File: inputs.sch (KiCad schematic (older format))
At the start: 72 parts, among them P29 .., P30 ., U4 MAX9926UAEE+, U5 74LS86, U6 MPX4100AP

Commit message: Updated Schematics, PDF, BOM for 4cyl Sequential Injection
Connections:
- wire segments 110 -> 109
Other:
- note added: "For Ford EDIS do not populate R64 and R65\nand connect U5 pins 5 and 6 to +5vdc\n(suggest using supply from U5 Pin 9)."
- note added: "For GM DIS and Ford EDIS leave Crank-IN- and Cam-IN- totally disconnected.\n\nFor Ford EDIS do not connect Cam-IN+ to anything either. \nR16, R17, C25, R10, R12 and D5 are not needed for the EDIS system.\n\nR20 and 23 are only to be used with VR Inputs, do not\npopulate these components for GM DIS or Ford EDIS systems."
- note added: "Power Supply For These Modules"
- note added: "R24, R25 and R31 should be replaced if using sensors other than\nGM temperature sensors.\nFor Ford use 27k 0.1% Metal Film resistors.\nFor Bosch and Nippon Denso use 2.2k 0.1% Metal Film resistors.\nFor Mopar use 9.31k 1% Metal Film resistors."
- note added: "Use the MPX4100AP for Non-Boosted Engines.\nUse the MPX4250AP for Boosted Engines."
- note removed: "At some point DIS Bypass needs to to be changed so that \nit only supplies +5vdc if RPM is greater than 400 RPM."
- moved on the sheet: C20, C21, C22, C23, C27, C28, C29, C30, C31, C32, C33, C34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

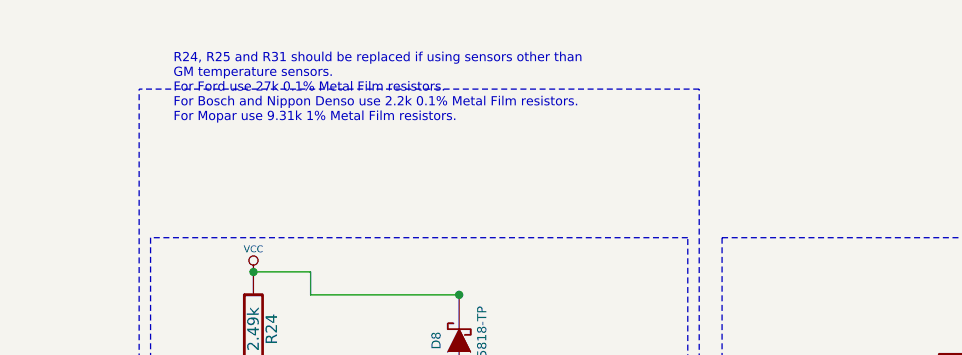
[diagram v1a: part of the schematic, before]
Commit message: Updated everything for up to 8 cylinder engines
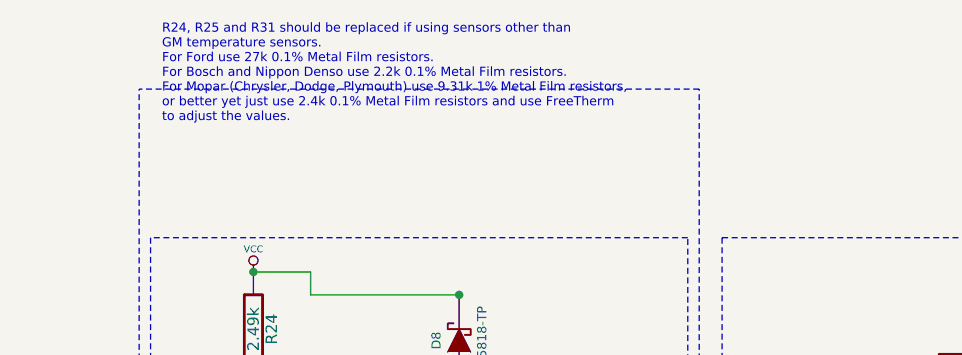
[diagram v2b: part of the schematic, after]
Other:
- note added: "R24, R25 and R31 should be replaced if using sensors other than\nGM temperature sensors.\nFor Ford use 27k 0.1% Metal Film resistors.\nFor Bosch and Nippon Denso use 2.2k 0.1% Metal Film resistors.\nFor Mopar (Chrysler, Dodge, Plymouth) use 9.31k 1% Metal Film resistors,\nor better yet just use 2.4k 0.1% Metal Film resistors and use FreeTherm\nto adjust the values."
- note removed: "R24, R25 and R31 should be replaced if using sensors other than\nGM temperature sensors.\nFor Ford use 27k 0.1% Metal Film resistors.\nFor Bosch and Nippon Denso use 2.2k 0.1% Metal Film resistors.\nFor Mopar use 9.31k 1% Metal Film resistors."
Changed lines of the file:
@@
-EESchema Schematic File Version 2  date Tue 24 Jan 2012 11:15:10 PM EST
+EESchema Schematic File Version 2  date Thu 26 Jan 2012 03:16:21 AM EST
 LIBS:power
 LIBS:device
@@
 Sheet 4 7
 Title "Jaguar PCB for FreeEMS"
-Date "25 jan 2012"
+Date "26 jan 2012"
 Rev "A.1"
 Comp "diyefi.org"
@@
 Text Notes 600  6200 0    40   ~ 0
 For Ford EDIS do not populate R64 and R65\nand connect U5 pins 5 and 6 to +5vdc\n(suggest using supply from U5 Pin 9).
-Text Notes 6100 750  0    40   ~ 0
-R24, R25 and R31 should be replaced if using sensors other than\nGM temperature sensors.\nFor Ford use 27k 0.1% Metal Film resistors.\nFor Bosch and Nippon Denso use 2.2k 0.1% Metal Film resistors.\nFor Mopar use 9.31k 1% Metal Film resistors.
+Text Notes 6050 750  0    40   ~ 0
+R24, R25 and R31 should be replaced if using sensors other than\nGM temperature sensors.\nFor Ford use 27k 0.1% Metal Film resistors.\nFor Bosch and Nippon Denso use 2.2k 0.1% Metal Film resistors.\nFor Mopar (Chrysler, Dodge, Plymouth) use 9.31k 1% Metal Film resistors,\nor better yet just use 2.4k 0.1% Metal Film resistors and use FreeTherm\nto adjust the values.
 Text Notes 650  750  0    40   ~ 0
 For GM DIS and Ford EDIS leave Crank-IN- and Cam-IN- totally disconnected.\n\nFor Ford EDIS do not connect Cam-IN+ to anything either. \nR16, R17, C25, R10, R12 and D5 are not needed for the EDIS system.\n\nR20 and 23 are only to be used with VR Inputs, do not\npopulate these components for GM DIS or Ford EDIS systems.
@@
 NoConn ~ 3600 5950
 $Comp
-L VCC #PWR029
+L VCC #PWR028
 U 1 1 4F1EDD96
 P 3600 5750
-F 0 "#PWR029" H 3600 5850 30  0001 C CNN
+F 0 "#PWR028" H 3600 5850 30  0001 C CNN
 F 1 "VCC" H 3600 5850 30  0000 C CNN
 	1    3600 5750
@@
 $EndComp
 $Comp
-L GND #PWR030
+L GND #PWR029
 U 1 1 4F1EDBE2
 P 900 5450
-F 0 "#PWR030" H 900 5450 30  0001 C CNN
+F 0 "#PWR029" H 900 5450 30  0001 C CNN
 F 1 "GND" H 900 5380 30  0001 C CNN
 	1    900  5450
@@
 $EndComp
 $Comp
-L VCC #PWR031
+L VCC #PWR030
 U 1 1 4F1EDBDA
 P 700 5400
-F 0 "#PWR031" H 700 5500 30  0001 C CNN
+F 0 "#PWR030" H 700 5500 30  0001 C CNN
 F 1 "VCC" H 700 5500 30  0000 C CNN
 	1    700  5400
@@
 JP1 and JP2 are to select \nnormal or inverting gates.
 $Comp
-L GND #PWR032
+L GND #PWR031
 U 1 1 4F1E9FBA
 P 2450 5150
-F 0 "#PWR032" H 2450 5150 30  0001 C CNN
+F 0 "#PWR031" H 2450 5150 30  0001 C CNN
 F 1 "GND" H 2450 5080 30  0001 C CNN
 	1    2450 5150
@@
 D4/R9 and D5/R10 are \nFor Diagnostics Only!\nIf they cause issues, \nremove them.
 $Comp
-L VCC #PWR033
+L VCC #PWR032
 U 1 1 4F1DC66C
 P 1250 3350
-F 0 "#PWR033" H 1250 3450 30  0001 C CNN
+F 0 "#PWR032" H 1250 3450 30  0001 C CNN
 F 1 "VCC" H 1250 3450 30  0000 C CNN
 	1    1250 3350
@@
 $EndComp
 $Comp
-L VCC #PWR034
+L VCC #PWR033
 U 1 1 4F1DC665
 P 1250 1450
-F 0 "#PWR034" H 1250 1550 30  0001 C CNN
+F 0 "#PWR033" H 1250 1550 30  0001 C CNN
 F 1 "VCC" H 1250 1550 30  0000 C CNN
 	1    1250 1450
@@
 Do NOT Connect Crank-IN- \nfor Hall/Opto/Digital
 $Comp
-L GND #PWR035
+L GND #PWR034
 U 1 1 4F1D8DAC
 P 1600 2800
-F 0 "#PWR035" H 1600 2800 30  0001 C CNN
+F 0 "#PWR034" H 1600 2800 30  0001 C CNN
 F 1 "GND" H 1600 2730 30  0001 C CNN
 	1    1600 2800
@@
 Crank-IN-
 $Comp
-L GND #PWR036
+L GND #PWR035
 U 1 1 4F1C330A
 P 4350 2650
-F 0 "#PWR036" H 4350 2650 30  0001 C CNN
+F 0 "#PWR035" H 4350 2650 30  0001 C CNN
 F 1 "GND" H 4350 2580 30  0001 C CNN
 	1    4350 2650
@@
 $EndComp
 $Comp
-L GND #PWR037
+L GND #PWR036
 U 1 1 4F1C32B6
 P 1700 1950
-F 0 "#PWR037" H 1700 1950 30  0001 C CNN
+F 0 "#PWR036" H 1700 1950 30  0001 C CNN
 F 1 "GND" H 1700 1880 30  0001 C CNN
 	1    1700 1950
@@
 $EndComp
 $Comp
-L VCC #PWR038
+L VCC #PWR037
 U 1 1 4F1C3261
 P 4350 2150
-F 0 "#PWR038" H 4350 2250 30  0001 C CNN
+F 0 "#PWR037" H 4350 2250 30  0001 C CNN
 F 1 "VCC" H 4350 2250 30  0000 C CNN
 	1    4350 2150
@@
 $EndComp
 $Comp
-L VCC #PWR039
+L VCC #PWR038
 U 1 1 4F1C325E
 P 4000 800
-F 0 "#PWR039" H 4000 900 30  0001 C CNN
+F 0 "#PWR038" H 4000 900 30  0001 C CNN
 F 1 "VCC" H 4000 900 30  0000 C CNN
 	1    4000 800
@@
 $EndComp
 $Comp
-L VCC #PWR040
+L VCC #PWR039
 U 1 1 4F1C3259
 P 1450 2950
-F 0 "#PWR040" H 1450 3050 30  0001 C CNN
+F 0 "#PWR039" H 1450 3050 30  0001 C CNN
 F 1 "VCC" H 1450 3050 30  0000 C CNN
 	1    1450 2950
@@
 $EndComp
 $Comp
-L VCC #PWR041
+L VCC #PWR040
 U 1 1 4F1C3254
 P 4000 4200
-F 0 "#PWR041" H 4000 4300 30  0001 C CNN
+F 0 "#PWR040" H 4000 4300 30  0001 C CNN
 F 1 "VCC" H 4000 4300 30  0000 C CNN
 	1    4000 4200
@@
 $EndComp
 $Comp
-L VCC #PWR042
+L VCC #PWR041
 U 1 1 4F1C3250
 P 1450 1850
-F 0 "#PWR042" H 1450 1950 30  0001 C CNN
+F 0 "#PWR041" H 1450 1950 30  0001 C CNN
 F 1 "VCC" H 1450 1950 30  0000 C CNN
 	1    1450 1850
@@
 P29 and P30 are for mounting holes for MPX4100AP
 $Comp
-L VCC #PWR043
+L VCC #PWR042
 U 1 1 4F1C302C
 P 4350 7350
-F 0 "#PWR043" H 4350 7450 30  0001 C CNN
+F 0 "#PWR042" H 4350 7450 30  0001 C CNN
 F 1 "VCC" H 4350 7450 30  0000 C CNN
 	1    4350 7350
@@
 $EndComp
 $Comp
-L GND #PWR044
+L GND #PWR043
 U 1 1 4F1C300F
 P 4450 7000
-F 0 "#PWR044" H 4450 7000 30  0001 C CNN
+F 0 "#PWR043" H 4450 7000 30  0001 C CNN
 F 1 "GND" H 4450 6930 30  0001 C CNN
 	1    4450 7000
@@
 $EndComp
 $Comp
-L GND #PWR045
+L GND #PWR044
 U 1 1 4F1C2FFA
 P 10350 3850
-F 0 "#PWR045" H 10350 3850 30  0001 C CNN
+F 0 "#PWR044" H 10350 3850 30  0001 C CNN
 F 1 "GND" H 10350 3780 30  0001 C CNN
 	1    10350 3850
@@
 $EndComp
 $Comp
-L GND #PWR046
+L GND #PWR045
 U 1 1 4F1C2FE3
 P 10350 2300
-F 0 "#PWR046" H 10350 2300 30  0001 C CNN
+F 0 "#PWR045" H 10350 2300 30  0001 C CNN
 F 1 "GND" H 10350 2230 30  0001 C CNN
 	1    10350 2300
@@
 $EndComp
 $Comp
-L VCC #PWR047
+L VCC #PWR046
 U 1 1 4F1C2FD7
 P 10050 1400
-F 0 "#PWR047" H 10050 1500 30  0001 C CNN
+F 0 "#PWR046" H 10050 1500 30  0001 C CNN
 F 1 "VCC" H 10050 1500 30  0000 C CNN
 	1    10050 1400
@@
 $EndComp
 $Comp
-L VCC #PWR048
+L VCC #PWR047
 U 1 1 4F1C2F9E
 P 10050 2950
-F 0 "#PWR048" H 10050 3050 30  0001 C CNN
+F 0 "#PWR047" H 10050 3050 30  0001 C CNN
 F 1 "VCC" H 10050 3050 30  0000 C CNN
 	1    10050 2950
@@
 $EndComp
 $Comp
-L VCC #PWR049
+L VCC #PWR048
 U 1 1 4F1C2F82
 P 10050 4750
-F 0 "#PWR049" H 10050 4850 30  0001 C CNN
+F 0 "#PWR048" H 10050 4850 30  0001 C CNN
 F 1 "VCC" H 10050 4850 30  0000 C CNN
 	1    10050 4750
@@
 $EndComp
 $Comp
-L GND #PWR050
+L GND #PWR049
 U 1 1 4F1C2F74
 P 8850 5800
-F 0 "#PWR050" H 8850 5800 30  0001 C CNN
+F 0 "#PWR049" H 8850 5800 30  0001 C CNN
 F 1 "GND" H 8850 5730 30  0001 C CNN
 	1    8850 5800
@@
 $EndComp
 $Comp
-L GND #PWR051
+L GND #PWR050
 U 1 1 4F1C2F64
 P 7750 5700
-F 0 "#PWR051" H 7750 5700 30  0001 C CNN
+F 0 "#PWR050" H 7750 5700 30  0001 C CNN
 F 1 "GND" H 7750 5630 30  0001 C CNN
 	1    7750 5700
@@
 $EndComp
 $Comp
-L VCC #PWR052
+L VCC #PWR051
 U 1 1 4F1C2F57
 P 6550 4700
-F 0 "#PWR052" H 6550 4800 30  0001 C CNN
+F 0 "#PWR051" H 6550 4800 30  0001 C CNN
 F 1 "VCC" H 6550 4800 30  0000 C CNN
 	1    6550 4700
@@
 This jumper allows us to \njump over Vcc on the PCB
 $Comp
-L VCC #PWR053
+L VCC #PWR052
 U 1 1 4F1C2F18
 P 6400 2950
-F 0 "#PWR053" H 6400 3050 30  0001 C CNN
+F 0 "#PWR052" H 6400 3050 30  0001 C CNN
 F 1 "VCC" H 6400 3050 30  0000 C CNN
 	1    6400 2950
@@
 $EndComp
 $Comp
-L GND #PWR054
+L GND #PWR053
 U 1 1 4F1C2F0A
 P 7600 3950
-F 0 "#PWR054" H 7600 3950 30  0001 C CNN
+F 0 "#PWR053" H 7600 3950 30  0001 C CNN
 F 1 "GND" H 7600 3880 30  0001 C CNN
 	1    7600 3950
@@
 $EndComp
 $Comp
-L GND #PWR055
+L GND #PWR054
 U 1 1 4F1C2EED
 P 7650 2400
-F 0 "#PWR055" H 7650 2400 30  0001 C CNN
+F 0 "#PWR054" H 7650 2400 30  0001 C CNN
 F 1 "GND" H 7650 2330 30  0001 C CNN
 	1    7650 2400
@@
 $EndComp
 $Comp
-L VCC #PWR056
+L VCC #PWR055
 U 1 1 4F1C2E50
 P 6450 1400
-F 0 "#PWR056" H 6450 1500 30  0001 C CNN
+F 0 "#PWR055" H 6450 1500 30  0001 C CNN
 F 1 "VCC" H 6450 1500 30  0000 C CNN
 	1    6450 1400
@@
 $EndComp
 $Comp
-L VCC #PWR057
+L VCC #PWR056
 U 1 1 4F1C2E3A
 P 1700 7100
-F 0 "#PWR057" H 1700 7200 30  0001 C CNN
+F 0 "#PWR056" H 1700 7200 30  0001 C CNN
 F 1 "VCC" H 1700 7200 30  0000 C CNN
 	1    1700 7100
@@
 $EndComp
 $Comp
-L VCC #PWR058
+L VCC #PWR057
 U 1 1 4F1C2E1E
 P 3600 5350
-F 0 "#PWR058" H 3600 5450 30  0001 C CNN
+F 0 "#PWR057" H 3600 5450 30  0001 C CNN
 F 1 "VCC" H 3600 5450 30  0000 C CNN
 	1    3600 5350
@@
 $EndComp
 $Comp
-L GND #PWR059
+L GND #PWR058
 U 1 1 4F1C2DD9
 P 2350 6050
-F 0 "#PWR059" H 2350 6050 30  0001 C CNN
+F 0 "#PWR058" H 2350 6050 30  0001 C CNN
 F 1 "GND" H 2350 5980 30  0001 C CNN
 	1    2350 6050
@@
 $EndComp
 $Comp
-L VCC #PWR060
+L VCC #PWR059
 U 1 1 4F1C2D2C
 P 2250 5100
-F 0 "#PWR060" H 2250 5200 30  0001 C CNN
+F 0 "#PWR059" H 2250 5200 30  0001 C CNN
 F 1 "VCC" H 2250 5200 30  0000 C CNN
 	1    2250 5100
